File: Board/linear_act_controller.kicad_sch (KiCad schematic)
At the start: 16 parts, among them J3 PROG, U1 STM32F030K6Tx

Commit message: Routing mostly done
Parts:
- removed C3, C4, C5: 100n, Capacitor_SMD:C_0603_1608Metric, symbol Device:C_Small
- removed D2: DBG, LED_SMD:LED_0603_1608Metric, symbol Device:LED_Small
- removed FB1, FB2: BLM18PG471SN1D, Inductor_SMD:L_0603_1608Metric, symbol Device:FerriteBead_Small
- removed R1, R2: 10k, Resistor_SMD:R_0603_1608Metric, symbol Device:R_Small
- removed R4: 1k, Resistor_SMD:R_0603_1608Metric, symbol Device:R_Small
- removed TP2: DBG, TestPoint:TestPoint_Pad_D1.0mm, symbol Connector:TestPoint
- removed U1: STM32F030K6Tx, Package_QFP:LQFP-32_7x7mm_P0.8mm, symbol MCU_ST_STM32F0:STM32F030K6Tx
- added C25, C26: 100n/100V, Capacitor_SMD:C_0603_1608Metric, symbol Device:C_Small
- added J1: SSV, symbol Connector:Conn_01x05_Pin
- added J2: ACTUATOR, symbol Connector:Conn_01x05_Pin
- added R15, R19: 58k, Resistor_SMD:R_0603_1608Metric, symbol Device:R_Small
- added R17, R20: 10k, Resistor_SMD:R_0603_1608Metric, symbol Device:R_Small
- J3: now fitted
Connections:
- net GND: now also C25.2, C26.2, J1.4 (Pin_4), J1.5 (Pin_5), J2.5 (Pin_5), R17.2, R20.2
- new net: J2.4 (Pin_4), R19.1
- new net: J1.3 (Pin_3), R15.1
- new net +24V: J1.2 (Pin_2), J2.3 (Pin_3)
- new net CONTROL_POT: C25.1, R15.2, R17.1
- new net OUT1: J2.1 (Pin_1)
- new net OUT2: J2.2 (Pin_2)
- new net POSITION_POT: C26.1, R19.2, R20.1
- new net VIN: J1.1 (Pin_1)
- no-connect marks 15 -> 1
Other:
- added sheet uC (uC.kicad_sch)
- note added: "PROG"
- note added: "To SSV"
- note added: "To actuator"
- note removed: "ADC_IN0"
- note removed: "TIM3_CH1"
- note removed: "TIM3_CH2"
- note removed: "TIM3_CH3"
- note removed: "TIM3_CH4"
- note removed: "uC"
- moved on the sheet: R12, R13, R14, R9

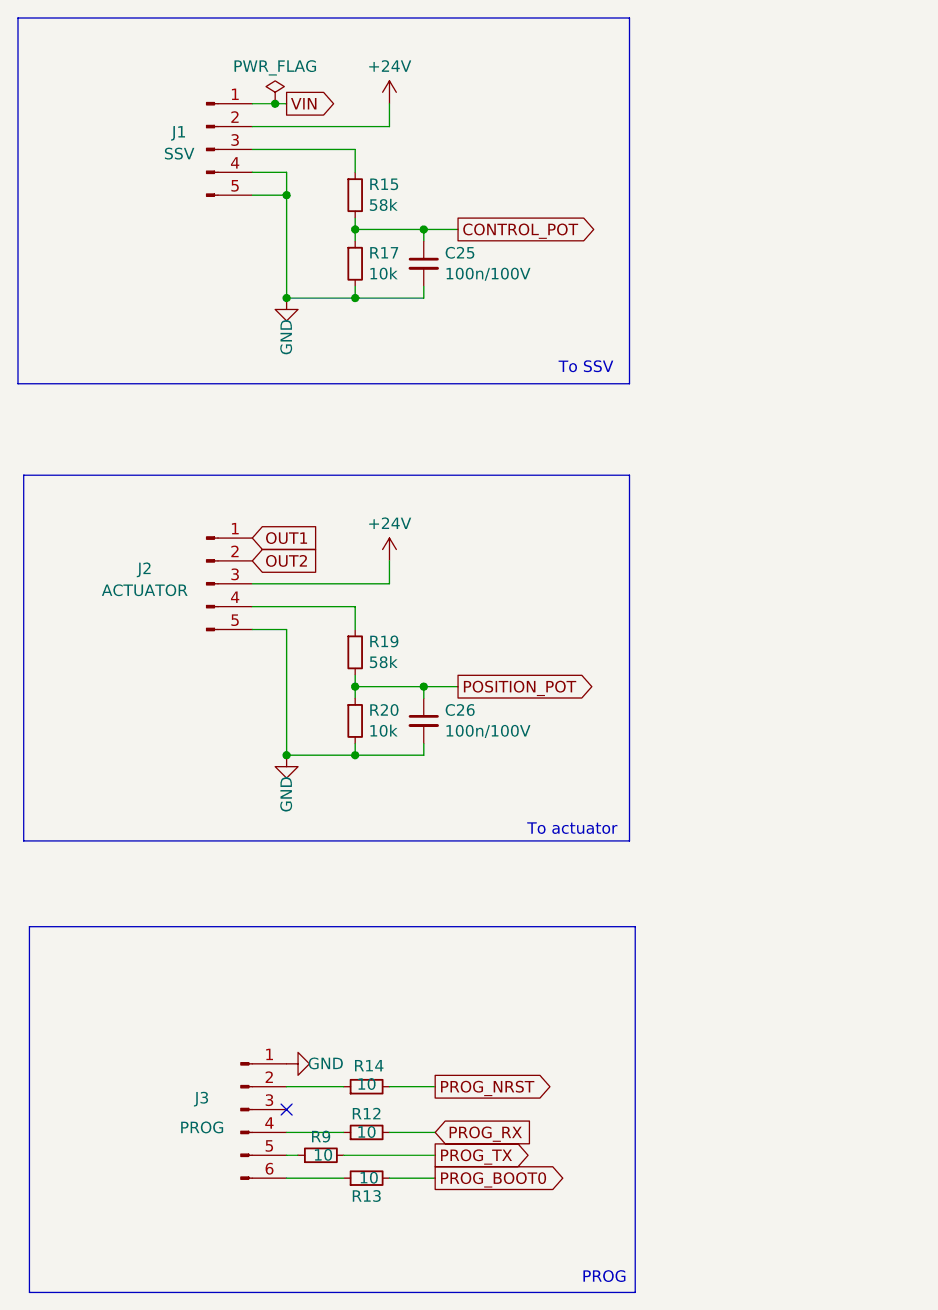
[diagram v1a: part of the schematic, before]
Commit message: Included jdam's improvements.
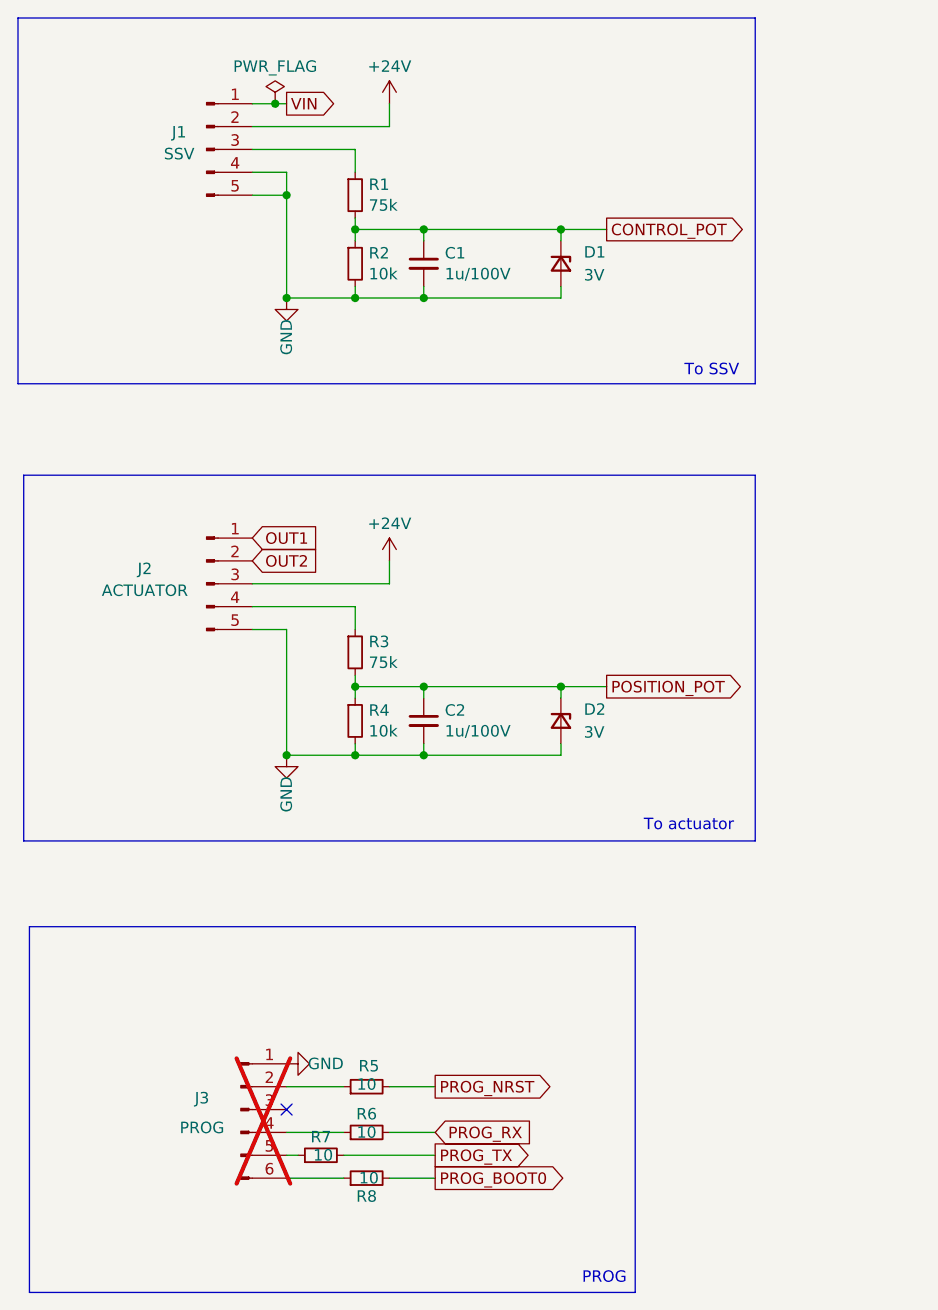
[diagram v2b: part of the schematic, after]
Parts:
- removed R19: 58k, Resistor_SMD:R_0603_1608Metric, symbol Device:R_Small
- added D1, D2: 3V, Diode_SMD:D_SOD-323_HandSoldering, symbol Device:D_Zener_Small
- added R3: 75k, Resistor_SMD:R_0603_1608Metric_Pad0.98x0.95mm_HandSolder, symbol Device:R_Small
- C1: renamed from C25; value 100n/100V -> 1u/100V; footprint Capacitor_SMD:C_0603_1608Metric -> Capacitor_SMD:C_0603_1608Metric_Pad1.08x0.95mm_HandSolder
- C2: renamed from C26; value 100n/100V -> 1u/100V; footprint Capacitor_SMD:C_0603_1608Metric -> Capacitor_SMD:C_0603_1608Metric_Pad1.08x0.95mm_HandSolder
- J1, J2: footprint (none) -> Connector_JST:JST_XH_B5B-XH-A_1x05_P2.50mm_Vertical
- J3: now not fitted
- R1: renamed from R15; value 58k -> 75k; footprint Resistor_SMD:R_0603_1608Metric -> Resistor_SMD:R_0603_1608Metric_Pad0.98x0.95mm_HandSolder
- R2: renamed from R17; footprint Resistor_SMD:R_0603_1608Metric -> Resistor_SMD:R_0603_1608Metric_Pad0.98x0.95mm_HandSolder
- R4: renamed from R20; footprint Resistor_SMD:R_0603_1608Metric -> Resistor_SMD:R_0603_1608Metric_Pad0.98x0.95mm_HandSolder
- R5: renamed from R14; footprint Resistor_SMD:R_0603_1608Metric -> Resistor_SMD:R_0603_1608Metric_Pad0.98x0.95mm_HandSolder
- R6: renamed from R12; footprint Resistor_SMD:R_0603_1608Metric -> Resistor_SMD:R_0603_1608Metric_Pad0.98x0.95mm_HandSolder
- R7: renamed from R9; footprint Resistor_SMD:R_0603_1608Metric -> Resistor_SMD:R_0603_1608Metric_Pad0.98x0.95mm_HandSolder
- R8: renamed from R13; footprint Resistor_SMD:R_0603_1608Metric -> Resistor_SMD:R_0603_1608Metric_Pad0.98x0.95mm_HandSolder
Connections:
- net CONTROL_POT: now also D1.1 (K)
- net GND: now also D1.2 (A), D2.2 (A)
- net POSITION_POT: now also D2.1 (K), R3.2
- net at J2.4 (Pin_4): now also R3.1

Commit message: WIP on routing
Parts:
- added H1, H2, H3, H4: MountingHole_Pad, MountingHole:MountingHole_3.5mm_Pad_Via, symbol Mechanical:MountingHole_Pad
- added J4: PWR_LED, Connector_JST:JST_XH_B2B-XH-A_1x02_P2.50mm_Vertical, symbol Connector:Conn_01x02_Pin
- added J5: STATUS_LED, Connector_JST:JST_XH_B2B-XH-A_1x02_P2.50mm_Vertical, symbol Connector:Conn_01x02_Pin
- added Q9: IRLML6344TRPBF, Package_TO_SOT_SMD:SOT-23_Handsoldering, symbol Transistor_FET:IRLML2060
- added R16, R24: 120, Resistor_SMD:R_0603_1608Metric_Pad0.98x0.95mm_HandSolder, symbol Device:R_Small
- added R36: 10k, Resistor_SMD:R_0603_1608Metric_Pad0.98x0.95mm_HandSolder, symbol Device:R
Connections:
- net GND: now also H1.1, H2.1, H3.1, H4.1, J4.2 (Pin_2), Q9.2 (S), R36.1
- new net: J5.1 (Pin_1), R24.2
- new net: J5.2 (Pin_2), Q9.3 (D)
- new net: J4.1 (Pin_1), R16.2
- new net +3.3V: R16.1, R24.1
- new net STATUS_LED: Q9.1 (G), R36.2
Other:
- note added: "https://www.mouser.fr/ProductDetail/Dialight/559-2201-001F?qs=DVhSRDYZfLoA%2F2lHATLc%252Bw%3D%3D"

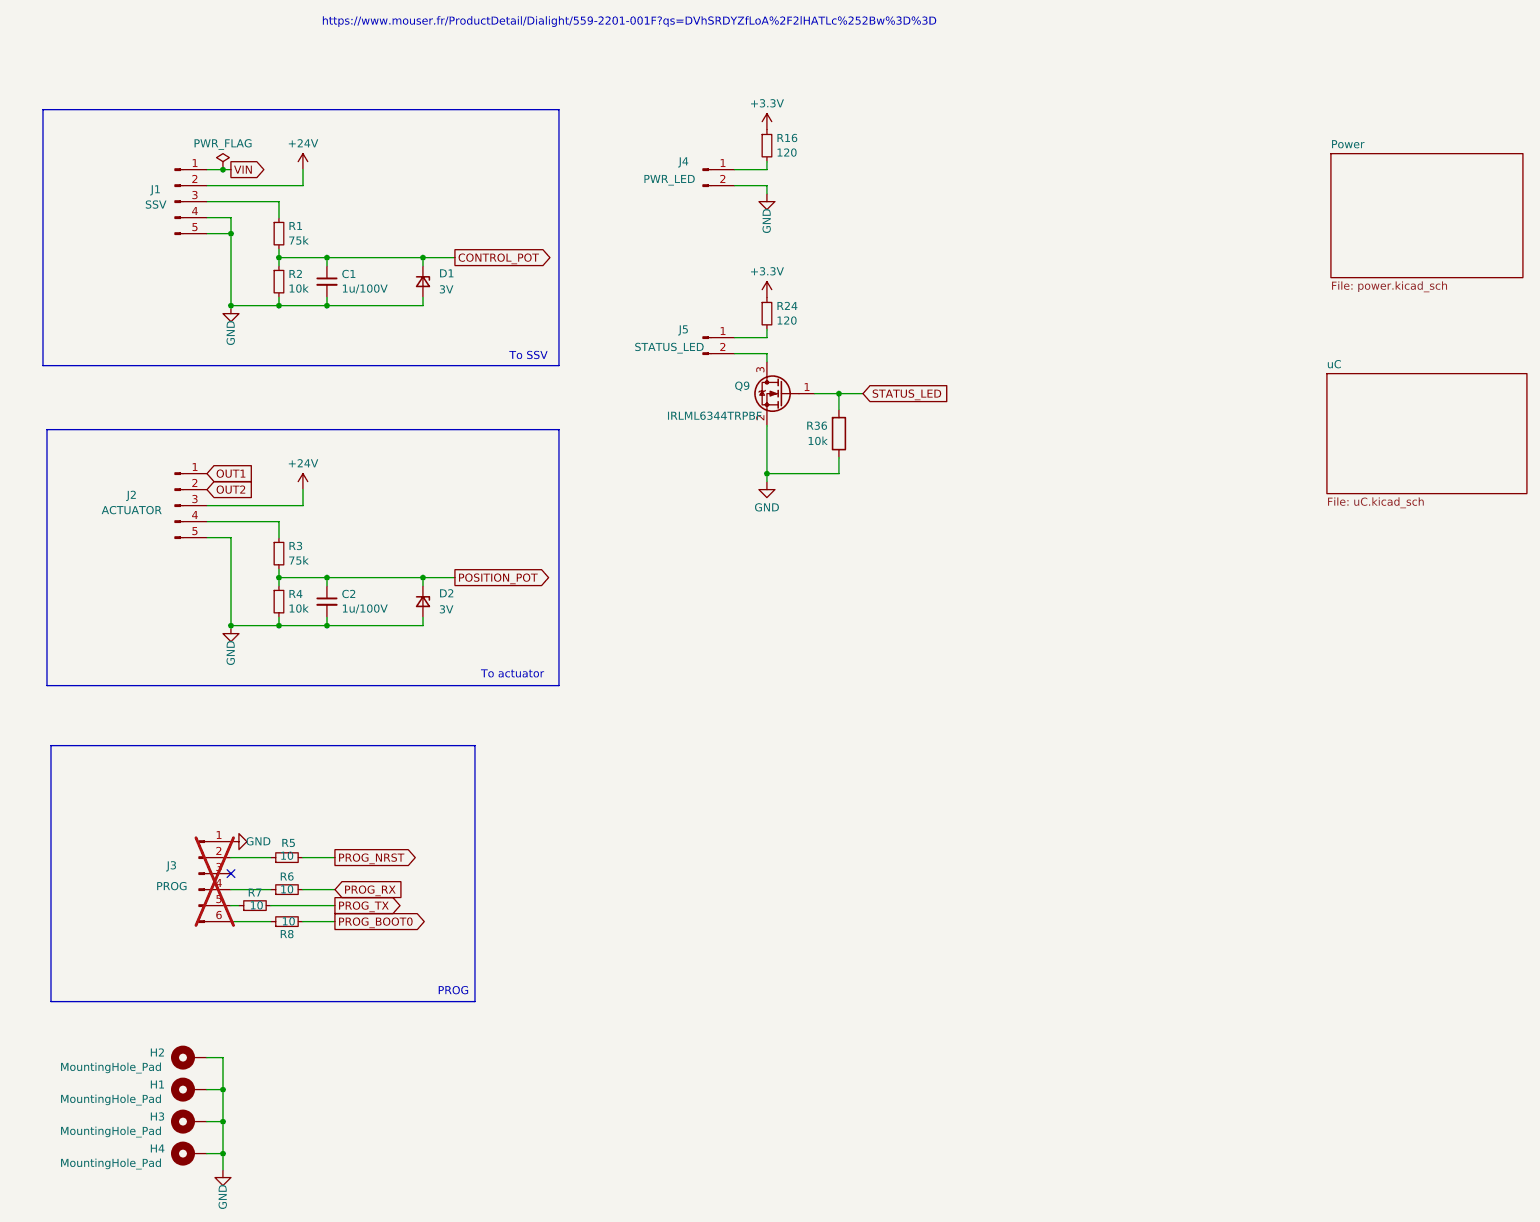
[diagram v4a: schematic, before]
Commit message: Routing done with polyfuse. Need to tidy silkscreen.
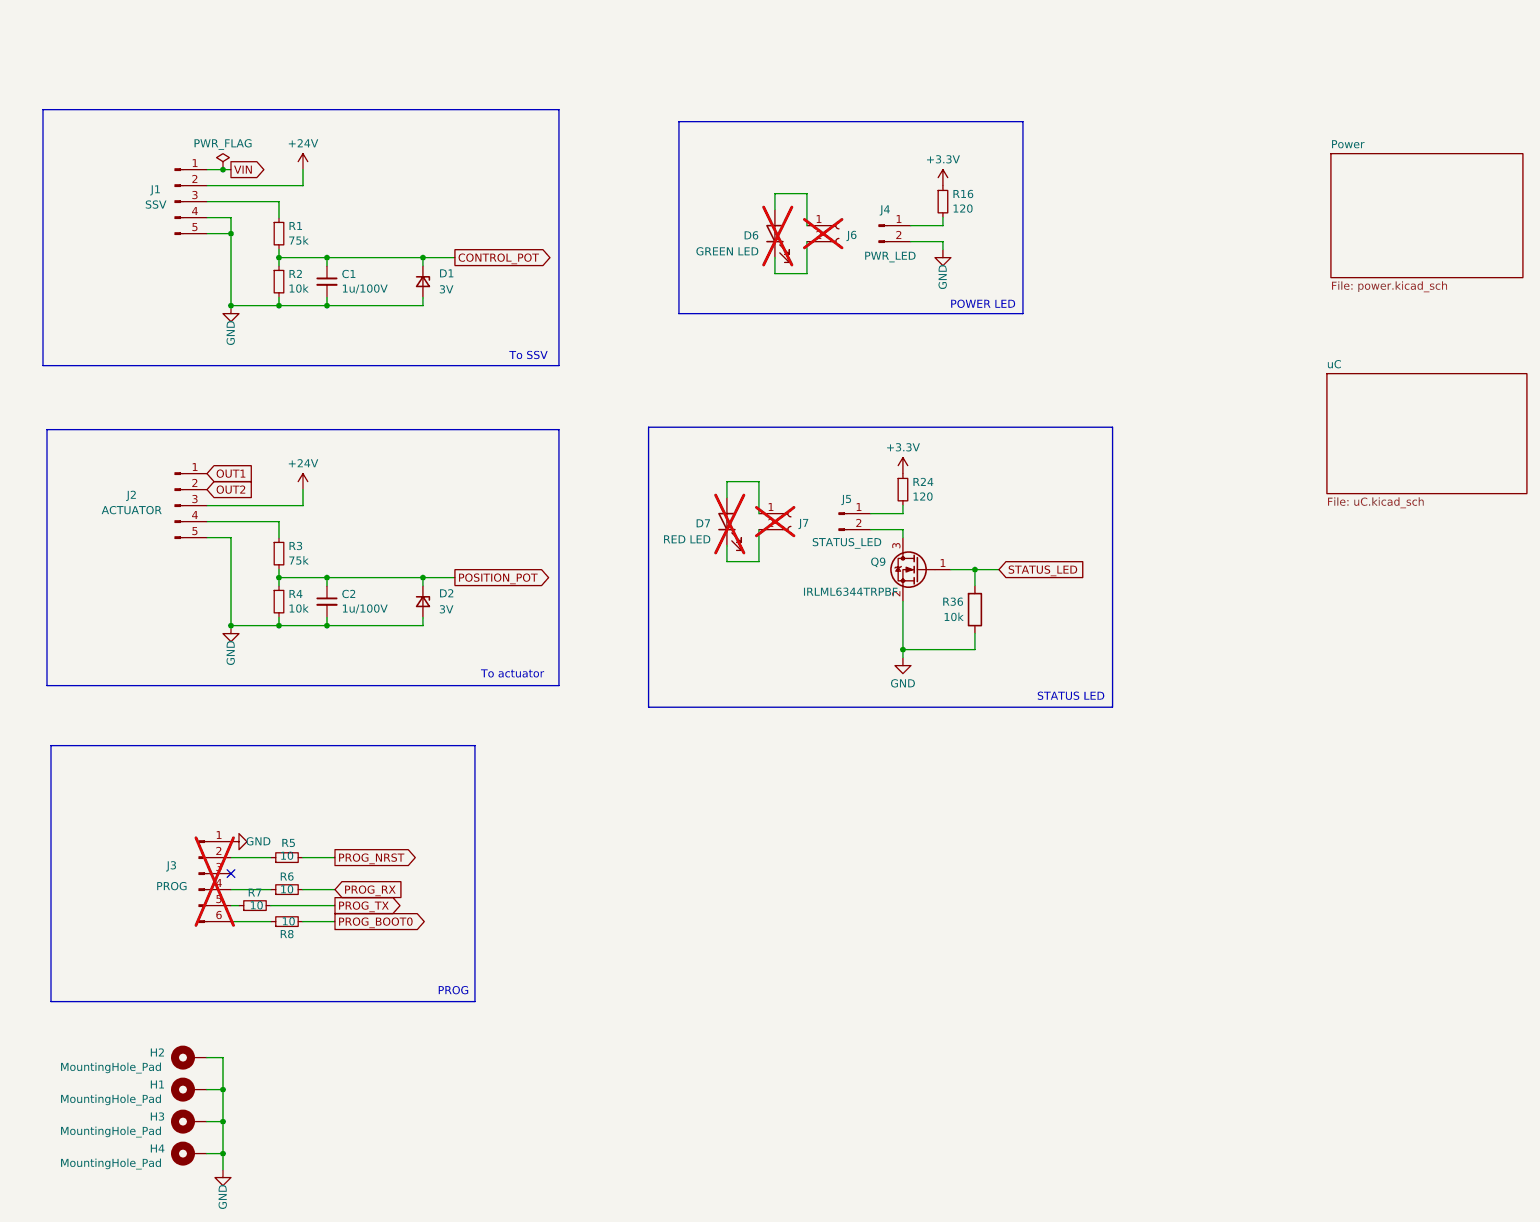
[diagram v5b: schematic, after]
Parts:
- added D6: GREEN LED, symbol Device:LED
- added D7: RED LED, symbol Device:LED
- added J6, J7: PWR_LED, symbol Connector:Conn_01x02_Socket
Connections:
- new net: D7.2 (A), J7.1 (Pin_1)
- new net: D7.1 (K), J7.2 (Pin_2)
- new net: D6.2 (A), J6.1 (Pin_1)
- new net: D6.1 (K), J6.2 (Pin_2)
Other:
- note added: "POWER LED"
- note added: "STATUS LED"
- note removed: "https://www.mouser.fr/ProductDetail/Dialight/559-2201-001F?qs=DVhSRDYZfLoA%2F2lHATLc%252Bw%3D%3D"
- moved on the sheet: J4, J5, Q9, R16, R24, R36
